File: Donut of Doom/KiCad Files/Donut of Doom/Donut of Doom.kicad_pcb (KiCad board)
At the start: 2 copper layers, 33.7 x 53 mm, 48 parts, among them Q1 Q_NMOS_GSD, U3 H3LIS331DLTR, U4 H3LIS331DLTR

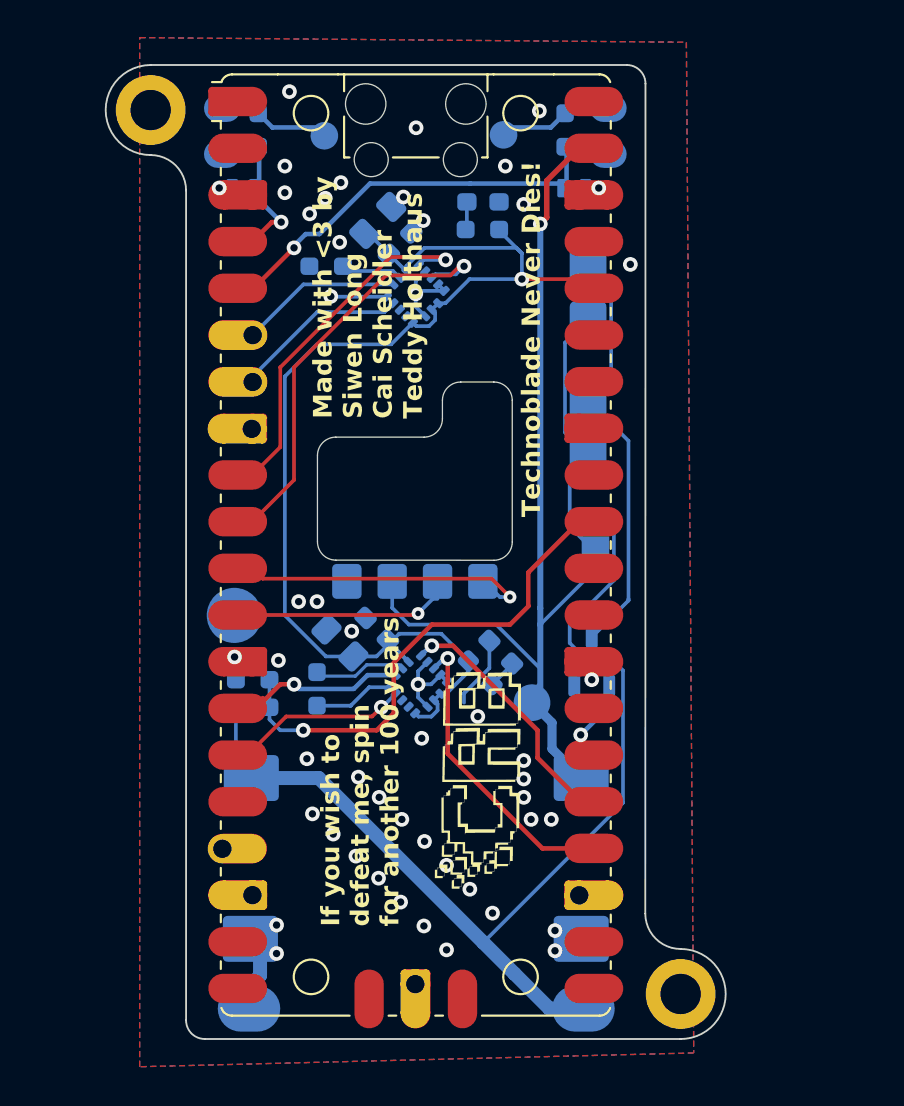
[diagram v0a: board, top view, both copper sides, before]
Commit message: fixed accelerameter positons
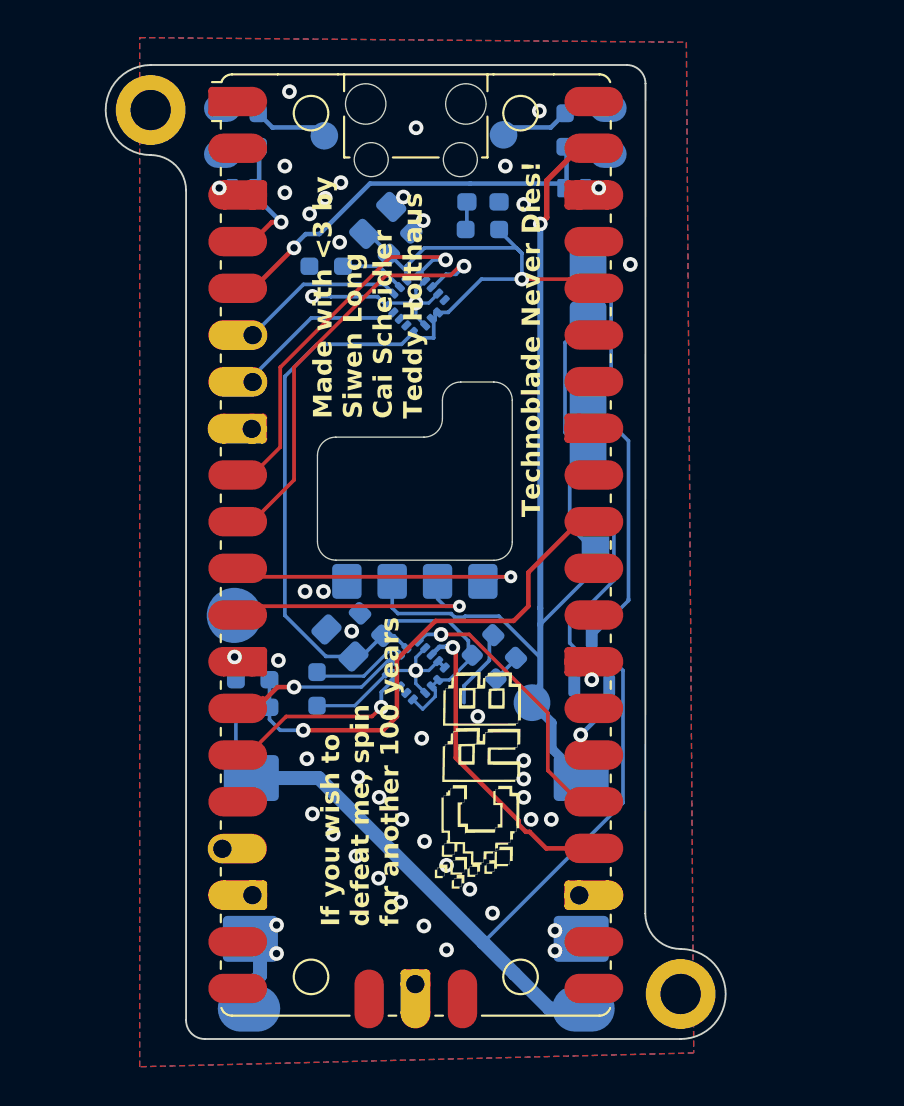
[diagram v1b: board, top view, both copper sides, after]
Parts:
- moved U4 0.76 mm to (150.6, 101.5)
- moved U3 0.50 mm to (150.6, 81.5)
- moved C4 0.39 mm to (148.2, 99.0)
- moved D7 0.37 mm to (155.5, 100.2)
- moved R9 0.37 mm to (154.3, 101.3)
- moved G*** 0.20 mm to (154.6, 82.8)
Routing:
- net GND: track 25.9 -> 30.2 mm
- net Net-(A1-GPIO9): track 10.4 -> 12.8 mm
- net /Lower INT2: track 13.3 -> 14.5 mm
- net +3V3: track 66.8 -> 67.8 mm
- net /Lower INT1: track 15.5 -> 16.3 mm
- net /I2C1 SCL: track 9.33 -> 10.0 mm
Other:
- board text added: "Donut of Doom PCB V3.1.1"
- board text removed: "Donut of Doom PCB V3"

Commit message: New resistor calculations for 6s HV
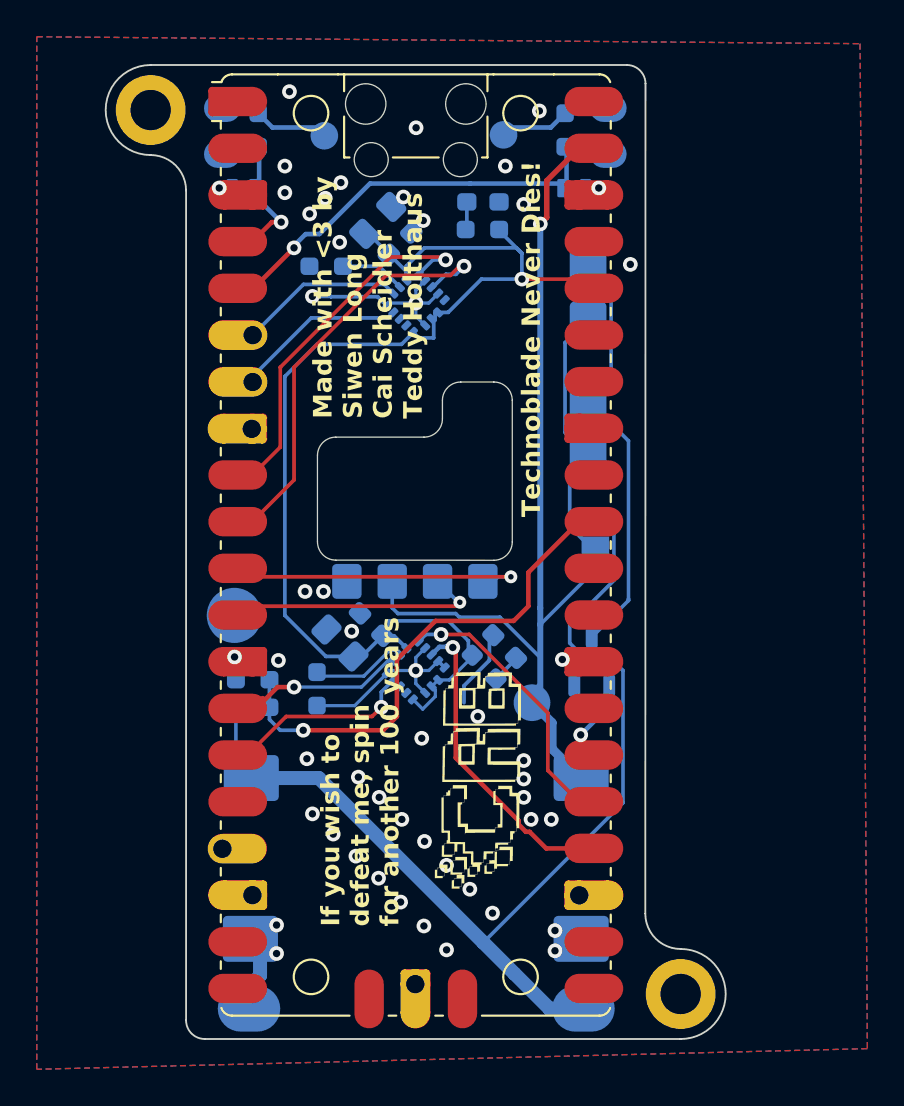
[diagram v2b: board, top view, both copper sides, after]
